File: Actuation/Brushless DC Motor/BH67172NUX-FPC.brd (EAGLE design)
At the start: 5 parts, among them IC1 BH67172NUX, IC2 BH67172NUX

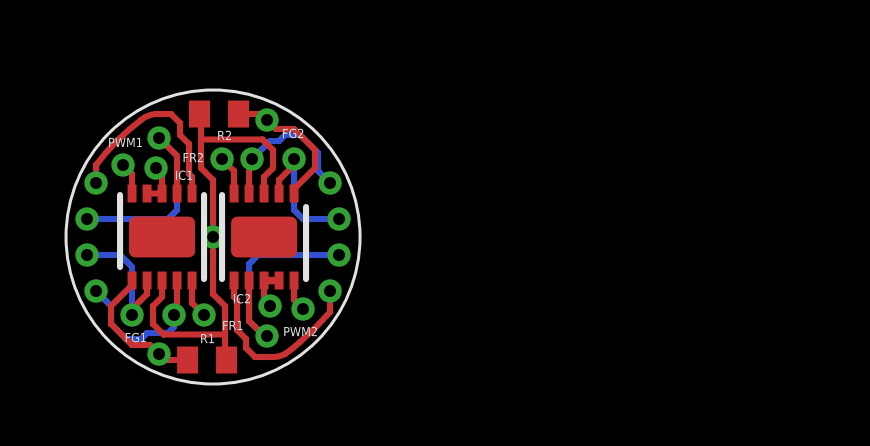
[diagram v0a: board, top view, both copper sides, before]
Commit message: Added BH67172NUX-FPC reference design
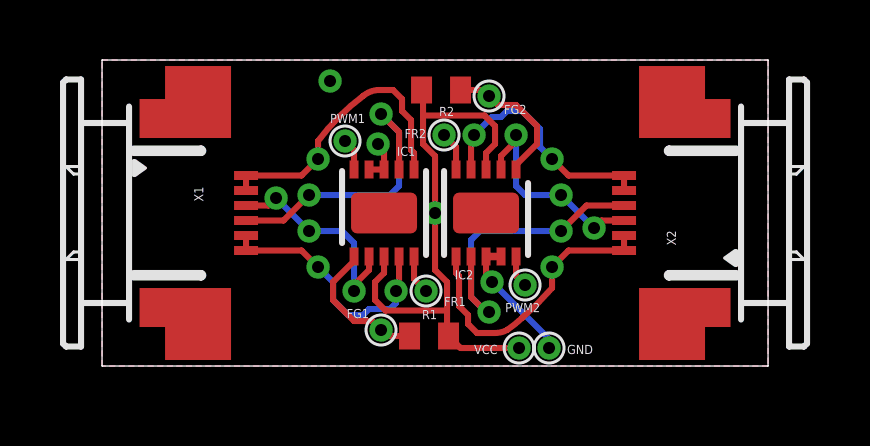
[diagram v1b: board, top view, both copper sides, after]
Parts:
- added X1, X2: 52745-0690, con-molex:52745-0690
- moved GOLD_ORB_SM1 15.8 mm to (28.5, 3.30)
- moved IC1 7.44 mm to (12.0, 6.60)
- moved IC2 7.44 mm to (15.4, 6.60)
- moved R1 7.44 mm to (13.5, 2.50)
- moved R2 7.44 mm to (13.9, 10.7)
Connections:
- net COM1: now also X1.3
- net COM2: now also X2.3
- net U1: now also X1.5, X1.6
- net U2: now also X2.5, X2.6
- net V1: now also X1.4
- net V2: now also X2.4
- net W1: now also X1.1, X1.2
- net W2: now also X2.1, X2.2
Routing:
- net U2: track 5.14 -> 8.26 mm
- net W2: track 6.61 -> 9.73 mm
- net U1: track 5.37 -> 8.50 mm
- net W1: track 6.70 -> 9.83 mm
- net GND: track 2.87 -> 5.85 mm, vias 2 -> 4
- net COM1: track 4.62 -> 7.28 mm, vias 2 -> 3
- net COM2: track 4.68 -> 7.34 mm, vias 2 -> 3
- net +3V3: track 16.8 -> 19.3 mm, vias 1 -> 2
- net V2: track 7.99 -> 10.4 mm
- net V1: track 7.87 -> 10.3 mm
- added copper zone on layer 1, net GND
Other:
- board outline added: 22.2 x 10.2 mm
